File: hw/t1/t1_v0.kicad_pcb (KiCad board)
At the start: 4 copper layers, 58 x 11.8 mm, 17 parts, among them J1 SFP_Module_Edge, J2 H-MTD PCB header (Rosenberger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, U1 DP83TG720S-Q1 / DP83TC812S-Q1, U2 STM32G031F6P6 (I2C slave: EEP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, U3 TPS62A01 3V3->1V0, Y1 25 MHz

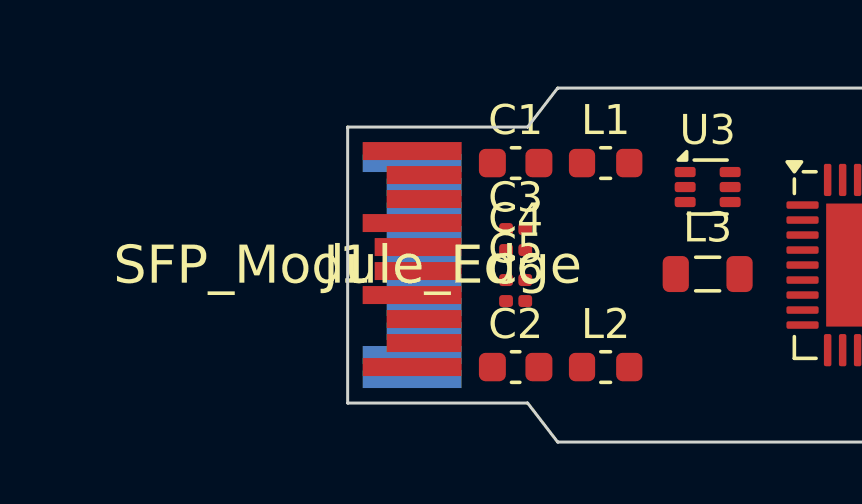
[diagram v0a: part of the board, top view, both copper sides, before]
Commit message: SFP edge was mirrored: fix the pad order, re-lay T1
The edge footprint put pin 20 at the top seen from above with the card edge
on the left; SFF-8419 Figure 7-2 (and INF-8074i Figure 2, drawn the other
way round) has pin 11 there. Every host contact would have landed between
two pads, VccT against ground. pad_y() is negated, the ground-finger vias
follow, and tools/compliance.py now states the expected positions itself.

T1, re-laid on the corrected edge:
- TD reaches the PHY's TX pins and RD its RX pins straight, P to P, both on
  top; the SGMII polarity-invert bits the firmware used to set are gone
- DP83TG720 EP 3.7 mm (RHA0036A), not 4.1
- XI series resistor R9: 0 ohm for the DP83TG720, 100 ohm in the DP83TC812
  loadout (SNLS654D Table 5-1)
- firmware clears SGMII AN on the DP83TC812 (SNLS654D 7.4.12.4)

Shared footprints: CMC land to TDK ACT1210E / Murata DLW32MH (1.05 x 0.6
pads, 0.4 between lines, 2.0 inner gap), H-MTD front solder area 2.2 wide
(MB_633), board thickness 1.0 mm in the files.

RJ45 and T1S still carry the mirrored edge; the README says not to order.
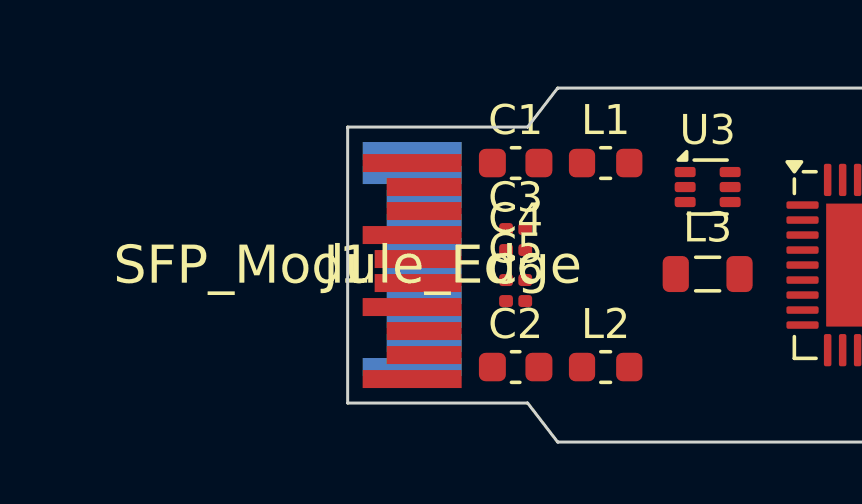
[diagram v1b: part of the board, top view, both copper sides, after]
